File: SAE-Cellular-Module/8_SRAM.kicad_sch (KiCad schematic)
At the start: 7 parts, among them U9 23K256T-I/ST

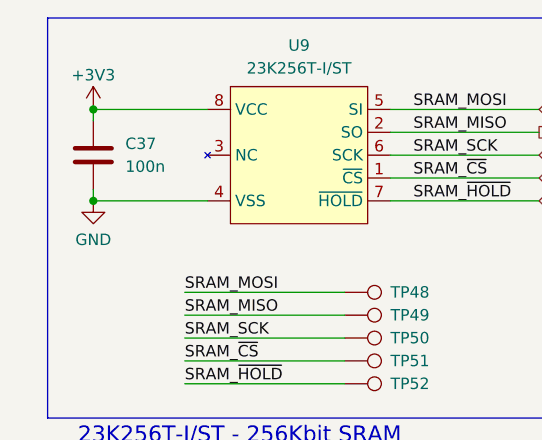
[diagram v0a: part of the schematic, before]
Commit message: Added initial component placements
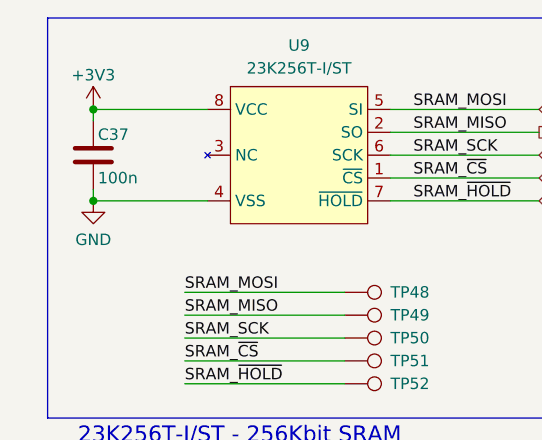
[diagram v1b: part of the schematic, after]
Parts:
- C37: footprint (none) -> Capacitor_SMD:C_0402_1005Metric; MPN (none) -> CL05B104KP5NNNC
- TP48, TP49, TP50, TP51, TP52: footprint (none) -> TestPoint:TestPoint_Pad_D1.0mm
- U9: MPN (none) -> 23K256T-I/ST
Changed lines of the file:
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@@
-	)
-	(symbol
-		(lib_id "Device:C")
-		(at 124.46 87.63 0)
-		(unit 1)
-		(exclude_from_sim no)
-		(in_bom yes)
-		(on_board yes)
-		(dnp no)
-		(property "Reference" "C37"
-			(at 128.016 86.36 0)
-			(effects
-				(font
-					(size 1.27 1.27)
-				)
-				(justify left)
-			)
-		)
-		(property "Value" "100n"
-			(at 128.016 88.9 0)
-			(effects
-				(font
-					(size 1.27 1.27)
-				)
-				(justify left)
-			)
-		)
-		(property "Footprint" ""
-			(at 125.4252 91.44 0)
-			(effects
-				(font
-					(size 1.27 1.27)
-				)
-				(hide yes)
-			)
-		)
-		(property "Datasheet" "~"
-			(at 124.46 87.63 0)
-			(effects
-				(font
-					(size 1.27 1.27)
-				)
-				(hide yes)
-			)
-		)
-		(property "Description" "Unpolarized capacitor"
-			(at 124.46 87.63 0)
-			(effects
-				(font
-					(size 1.27 1.27)
-				)
-				(hide yes)
-			)
-		)
-		(pin "1"
-		)
-		(pin "2"
-		)
-		(instances
-			(project ""
-				(path "/a08fab55-11db-44fb-b9aa-270892bf89c0/e38f8bc0-67b3-4584-95c9-b56f13e21511"
-					(reference "C37")
-					(unit 1)
-				)
-			)
-		)
 	)
 	(symbol
@@
 			)
 		)
-		(property "Footprint" ""
+		(property "Footprint" "TestPoint:TestPoint_Pad_D1.0mm"
 			(at 152.4 118.11 0)
 			(effects
@@
 		)
 		(property "Description" ""
+			(at 147.32 80.01 0)
+			(effects
+				(font
+					(size 1.27 1.27)
+				)
+				(hide yes)
+			)
+		)
+		(property "MPN" "23K256T-I/ST"
 			(at 147.32 80.01 0)
 			(effects
@@
 			)
 		)
-		(property "Footprint" ""
+		(property "Footprint" "TestPoint:TestPoint_Pad_D1.0mm"
 			(at 152.4 115.57 0)
 			(effects
@@
 			)
 		)
-		(property "Footprint" ""
+		(property "Footprint" "TestPoint:TestPoint_Pad_D1.0mm"
 			(at 152.4 113.03 0)
 			(effects
@@
 			)
 		)
-		(property "Footprint" ""
+		(property "Footprint" "TestPoint:TestPoint_Pad_D1.0mm"
 			(at 152.4 107.95 0)
 			(effects
@@
 			)
 		)
-		(property "Footprint" ""
+		(property "Footprint" "TestPoint:TestPoint_Pad_D1.0mm"
 			(at 152.4 110.49 0)
 			(effects
@@
 					(unit 1)
 				)
+			)
+		)
+	)
+	(symbol
+		(lib_id "Device:C")
+		(at 124.46 87.63 0)
+		(unit 1)
+		(exclude_from_sim no)
+		(in_bom yes)
+		(on_board yes)
+		(dnp no)
+		(property "Reference" "C37"
+			(at 124.968 85.344 0)
+			(effects
+				(font
+					(size 1.27 1.27)
+				)
+				(justify left)
+			)
+		)
+		(property "Value" "100n"
+			(at 124.968 90.17 0)
+			(effects
+				(font
+					(size 1.27 1.27)
+				)
+				(justify left)
+			)
+		)
+		(property "Footprint" "Capacitor_SMD:C_0402_1005Metric"
+			(at 125.4252 91.44 0)
+			(effects
+				(font
+					(size 1.27 1.27)
+				)
+				(hide yes)
+			)
+		)
+		(property "Datasheet" "~"
+			(at 124.46 87.63 0)
+			(effects
+				(font
+					(size 1.27 1.27)
+				)
+				(hide yes)
+			)
+		)
+		(property "Description" "Unpolarized capacitor"
+			(at 124.46 87.63 0)
+			(effects
+				(font
+					(size 1.27 1.27)
+				)
+				(hide yes)
+			)
+		)
+		(property "MPN" "CL05B104KP5NNNC"
+			(at 124.46 87.63 0)
+			(effects
+				(font
+					(size 1.27 1.27)
+				)
+				(hide yes)
+			)
+		)
+		(pin "2"
+		)
+		(pin "1"
+		)
+		(instances
+			(project "SAE Cellular Module"
+				(path "/a08fab55-11db-44fb-b9aa-270892bf89c0/e38f8bc0-67b3-4584-95c9-b56f13e21511"
+					(reference "C37")
+					(unit 1)
+				)
